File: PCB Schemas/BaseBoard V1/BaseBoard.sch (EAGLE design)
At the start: 31 parts, among them IC1 74HC595D, IC2 74HC595D, IC3 74HC595D, U1 ATMEGA2560AU, X1 16MHz

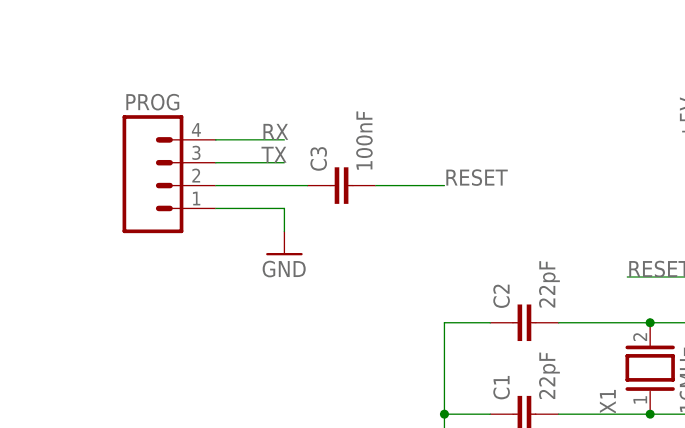
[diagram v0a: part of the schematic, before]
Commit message: Corrected BaseBoard V1 and updated license file
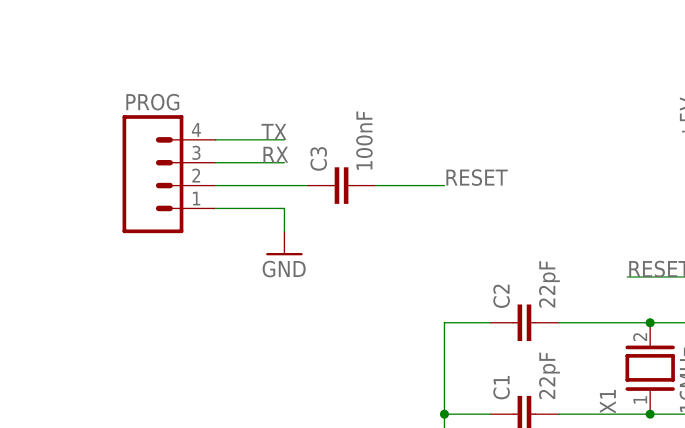
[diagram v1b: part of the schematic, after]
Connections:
- net RX: now also PROG.3; no longer PROG.4
- net TX: now also PROG.4; no longer PROG.3
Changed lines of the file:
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@@
 <net name="RX" class="0">
+<segment>
+<label x="132.08" y="-2.54" size="1.778" layer="95"/>
+<pinref part="U1" gate="1" pin="(RXD0/PCIN8)PE0"/>
+<wire x1="106.68" y1="-2.54" x2="132.08" y2="-2.54" width="0.1524" layer="91"/>
+</segment>
+<segment>
+<pinref part="PROG" gate="G$1" pin="3"/>
+<wire x1="-30.48" y1="119.38" x2="-22.86" y2="119.38" width="0.1524" layer="91"/>
+<label x="-25.4" y="119.38" size="1.778" layer="95"/>
+</segment>
+</net>
+<net name="TX" class="0">
+<segment>
+<label x="132.08" y="0" size="1.778" layer="95"/>
+<pinref part="U1" gate="1" pin="(TXD0)PE1"/>
+<wire x1="132.08" y1="0" x2="106.68" y2="0" width="0.1524" layer="91"/>
+</segment>
 <segment>
 <pinref part="PROG" gate="G$1" pin="4"/>
@@
 <label x="-25.4" y="121.92" size="1.778" layer="95"/>
 </segment>
-<segment>
-<label x="132.08" y="-2.54" size="1.778" layer="95"/>
-<pinref part="U1" gate="1" pin="(RXD0/PCIN8)PE0"/>
-<wire x1="106.68" y1="-2.54" x2="132.08" y2="-2.54" width="0.1524" layer="91"/>
-</segment>
 </net>
-<net name="TX" class="0">
-<segment>
-<pinref part="PROG" gate="G$1" pin="3"/>
-<wire x1="-30.48" y1="119.38" x2="-22.86" y2="119.38" width="0.1524" layer="91"/>
-<label x="-25.4" y="119.38" size="1.778" layer="95"/>
-</segment>
-<segment>
-<label x="132.08" y="0" size="1.778" layer="95"/>
-<pinref part="U1" gate="1" pin="(TXD0)PE1"/>
-<wire x1="132.08" y1="0" x2="106.68" y2="0" width="0.1524" layer="91"/>
-</segment>
-</net>

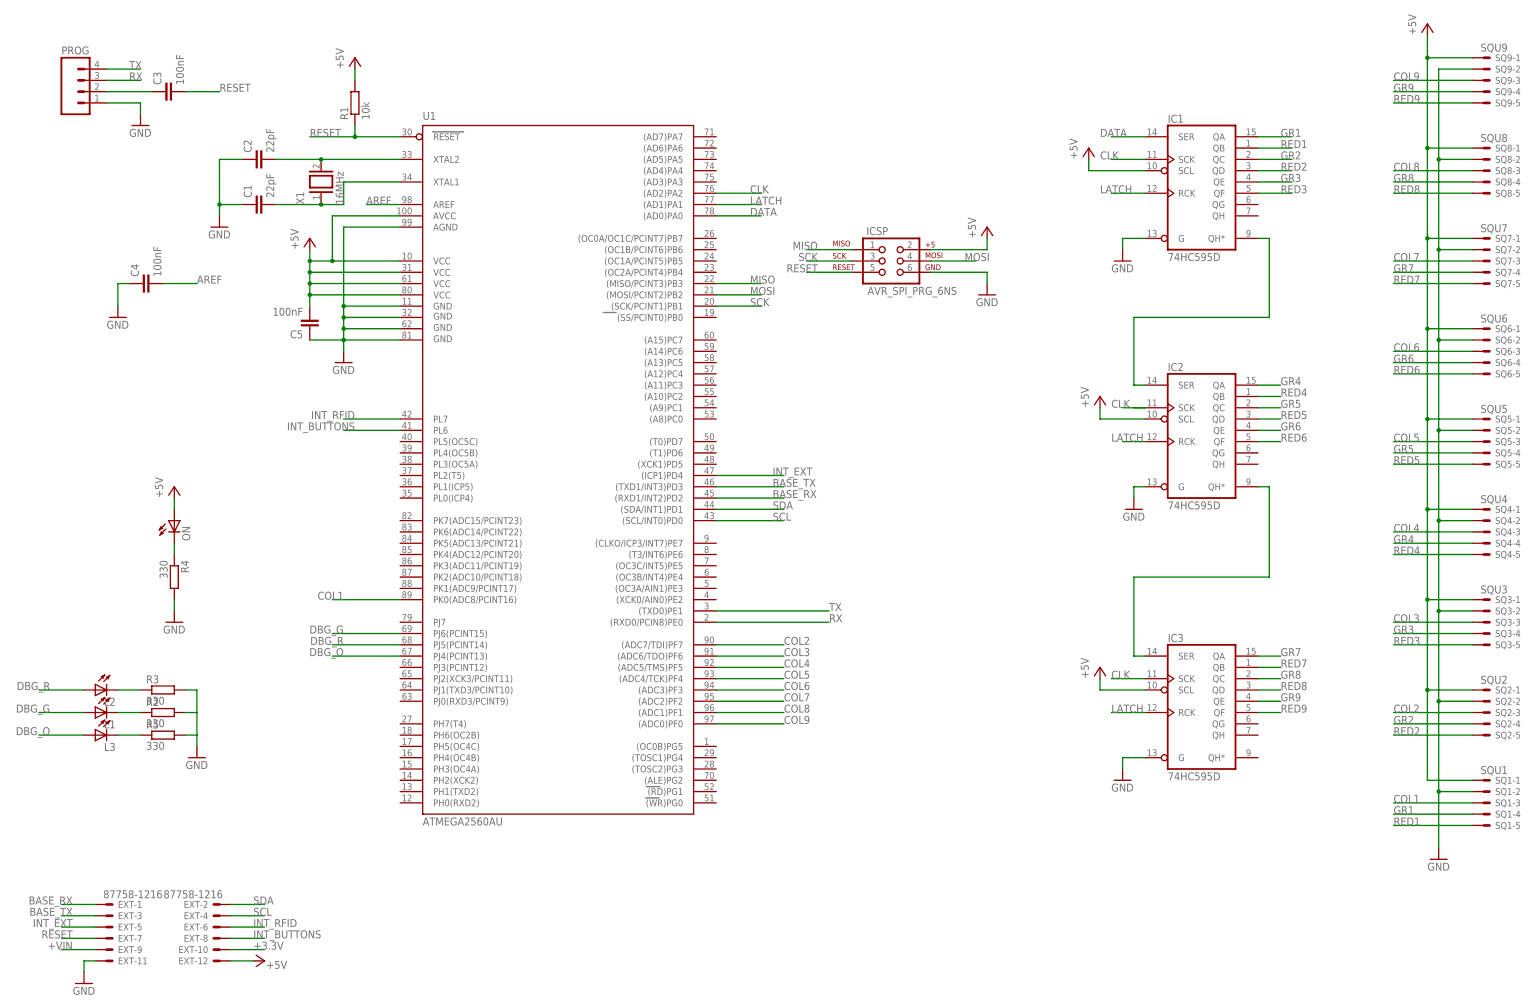
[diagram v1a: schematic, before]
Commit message: Modified base conector; delete reset pin
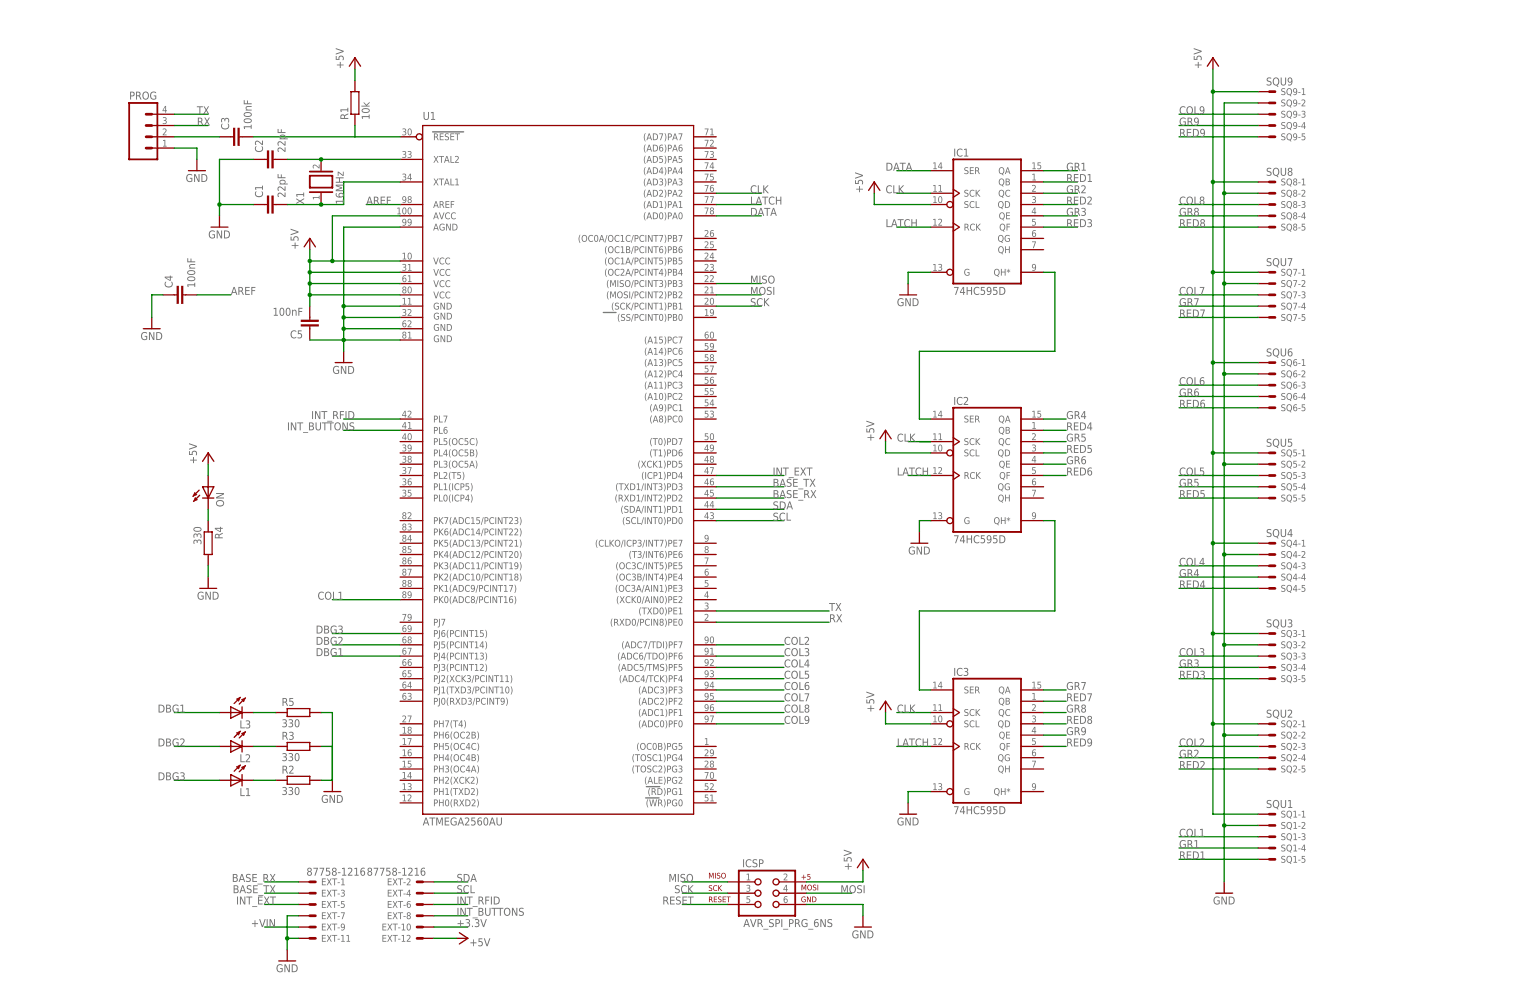
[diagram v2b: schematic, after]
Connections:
- net DBG_G renamed DBG3
- net DBG_O renamed DBG1
- net DBG_R renamed DBG2
- net GND: now also EXT-7.S
- net RESET: no longer EXT-7.S
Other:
- moved on the sheet: C1, C2, C3, C4, EXT-1, EXT-10, EXT-11, EXT-12, EXT-2, EXT-3, EXT-4, EXT-5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

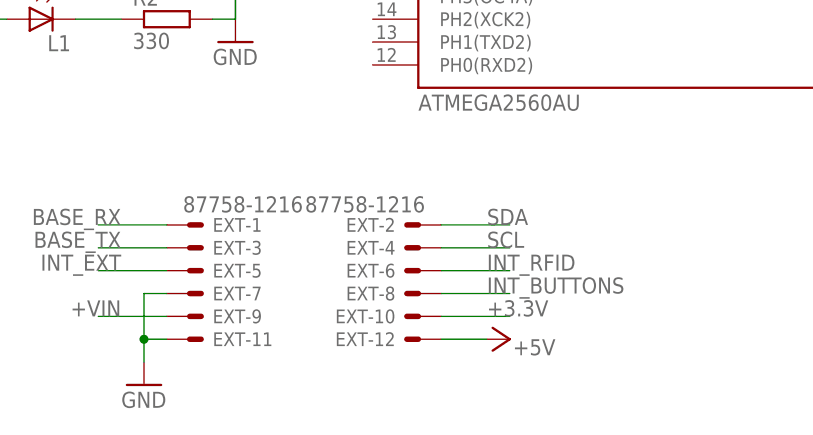
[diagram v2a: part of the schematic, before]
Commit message: Update base conector package
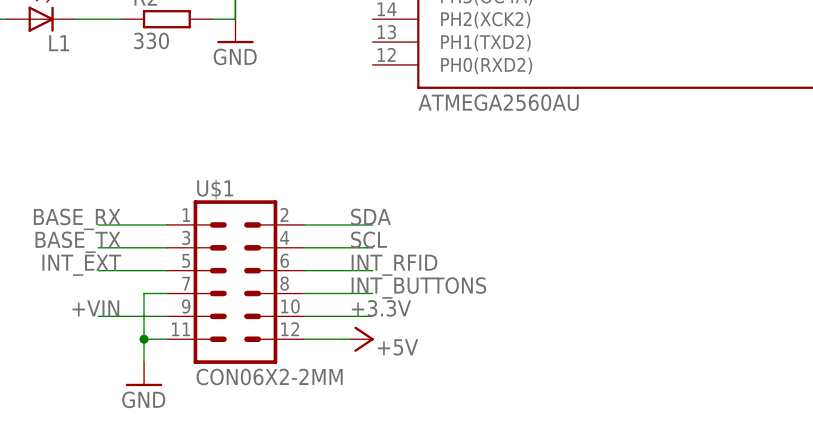
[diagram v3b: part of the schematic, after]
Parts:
- removed EXT: 87758-1216, con-molex:87758-1216
- added U$1: CON06X2-2MM, Connectors:CON06X2-2MM
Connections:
- net +3.3V: now also U$1.10; no longer EXT-10.S
- net +VIN: now also U$1.9; no longer EXT-9.S
- net BASE_RX: now also U$1.1; no longer EXT-1.S
- net BASE_TX: now also U$1.3; no longer EXT-3.S
- net GND: now also U$1.11, U$1.7; no longer EXT-11.S, EXT-7.S
- net INT_BUTTONS: now also U$1.8; no longer EXT-8.S
- net INT_EXT: now also U$1.5; no longer EXT-5.S
- net INT_RFID: now also U$1.6; no longer EXT-6.S
- net SCL: now also U$1.4; no longer EXT-4.S
- net SDA: now also U$1.2; no longer EXT-2.S
- net VCC: now also U$1.12; no longer EXT-12.S
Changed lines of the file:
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@@
 <part name="GND5" library="supply1" deviceset="GND" device=""/>
 <part name="P+3" library="supply1" deviceset="VCC" device="" value="+5V"/>
-<part name="EXT" library="con-molex" deviceset="87758-1216" device=""/>
 <part name="R2" library="resistor" deviceset="R-EU_" device="R0805" value="330"/>
 <part name="R3" library="resistor" deviceset="R-EU_" device="R0805" value="330"/>
@@
 <part name="L1" library="led" deviceset="LED" device="CHIP-LED0805"/>
 <part name="L3" library="led" deviceset="LED" device="CHIP-LED0805"/>
+<part name="U$1" library="Connectors" deviceset="CON06X2-2MM" device=""/>
 </parts>
 <sheets>
@@
 <instance part="GND11" gate="1" x="149.86" y="-45.72"/>
 <instance part="GND12" gate="1" x="10.16" y="-78.74"/>
-<instance part="P+9" gate="VCC" x="50.8" y="-73.66" smashed="yes" rot="R270">
-<attribute name="VALUE" x="55.88" y="-73.66" size="1.778" layer="96" rot="R180"/>
+<instance part="P+9" gate="VCC" x="35.56" y="-73.66" smashed="yes" rot="R270">
+<attribute name="VALUE" x="40.64" y="-73.66" size="1.778" layer="96" rot="R180"/>
 </instance>
 <instance part="ICSP" gate="G$1" x="116.84" y="-63.5"/>
 <instance part="GND5" gate="1" x="139.7" y="-71.12"/>
 <instance part="P+3" gate="VCC" x="139.7" y="-55.88"/>
-<instance part="EXT" gate="-1" x="15.24" y="-60.96"/>
-<instance part="EXT" gate="-2" x="40.64" y="-60.96" rot="MR0"/>
-<instance part="EXT" gate="-3" x="15.24" y="-63.5"/>
-<instance part="EXT" gate="-4" x="40.64" y="-63.5" rot="MR0"/>
-<instance part="EXT" gate="-5" x="15.24" y="-66.04"/>
-<instance part="EXT" gate="-6" x="40.64" y="-66.04" rot="MR0"/>
-<instance part="EXT" gate="-7" x="15.24" y="-68.58"/>
-<instance part="EXT" gate="-8" x="40.64" y="-68.58" rot="MR0"/>
-<instance part="EXT" gate="-9" x="15.24" y="-71.12"/>
-<instance part="EXT" gate="-10" x="40.64" y="-71.12" rot="MR0"/>
-<instance part="EXT" gate="-11" x="15.24" y="-73.66"/>
-<instance part="EXT" gate="-12" x="40.64" y="-73.66" rot="MR0"/>
 <instance part="R2" gate="G$1" x="12.7" y="-38.1"/>
 <instance part="R3" gate="G$1" x="12.7" y="-30.48"/>
@@
 <instance part="L1" gate="G$1" x="-2.54" y="-38.1" rot="MR270"/>
 <instance part="L3" gate="G$1" x="-2.54" y="-22.86" rot="MR270"/>
+<instance part="U$1" gate="G$1" x="20.32" y="-68.58"/>
 </instances>
 <busses>
@@
 <segment>
 <pinref part="P+9" gate="VCC" pin="VCC"/>
-<wire x1="43.18" y1="-73.66" x2="48.26" y2="-73.66" width="0.1524" layer="91"/>
-<pinref part="EXT" gate="-12" pin="S"/>
+<wire x1="27.94" y1="-73.66" x2="33.02" y2="-73.66" width="0.1524" layer="91"/>
+<pinref part="U$1" gate="G$1" pin="12"/>
 </segment>
 </net>
@@
 <wire x1="12.7" y1="-73.66" x2="10.16" y2="-73.66" width="0.1524" layer="91"/>
 <wire x1="10.16" y1="-73.66" x2="10.16" y2="-76.2" width="0.1524" layer="91"/>
-<pinref part="EXT" gate="-11" pin="S"/>
-<pinref part="EXT" gate="-7" pin="S"/>
 <wire x1="12.7" y1="-68.58" x2="10.16" y2="-68.58" width="0.1524" layer="91"/>
 <wire x1="10.16" y1="-68.58" x2="10.16" y2="-73.66" width="0.1524" layer="91"/>
 <junction x="10.16" y="-73.66"/>
+<pinref part="U$1" gate="G$1" pin="7"/>
+<pinref part="U$1" gate="G$1" pin="11"/>
 </segment>
 </net>
@@
 </segment>
 <segment>
-<wire x1="43.18" y1="-63.5" x2="50.8" y2="-63.5" width="0.1524" layer="91"/>
-<label x="48.26" y="-63.5" size="1.778" layer="95"/>
-<pinref part="EXT" gate="-4" pin="S"/>
+<wire x1="27.94" y1="-63.5" x2="35.56" y2="-63.5" width="0.1524" layer="91"/>
+<label x="33.02" y="-63.5" size="1.778" layer="95"/>
+<pinref part="U$1" gate="G$1" pin="4"/>
 </segment>
 </net>
@@
 </segment>
 <segment>
-<wire x1="43.18" y1="-60.96" x2="50.8" y2="-60.96" width="0.1524" layer="91"/>
-<label x="48.26" y="-60.96" size="1.778" layer="95"/>
-<pinref part="EXT" gate="-2" pin="S"/>
+<wire x1="27.94" y1="-60.96" x2="35.56" y2="-60.96" width="0.1524" layer="91"/>
+<label x="33.02" y="-60.96" size="1.778" layer="95"/>
+<pinref part="U$1" gate="G$1" pin="2"/>
 </segment>
 </net>
@@
 <wire x1="12.7" y1="-63.5" x2="5.08" y2="-63.5" width="0.1524" layer="91"/>
 <label x="7.62" y="-63.5" size="1.778" layer="95" rot="MR0"/>
-<pinref part="EXT" gate="-3" pin="S"/>
+<pinref part="U$1" gate="G$1" pin="3"/>
 </segment>
 </net>
@@
 <wire x1="12.7" y1="-60.96" x2="5.08" y2="-60.96" width="0.1524" layer="91"/>
 <label x="7.62" y="-60.96" size="1.778" layer="95" rot="MR0"/>
-<pinref part="EXT" gate="-1" pin="S"/>
+<pinref part="U$1" gate="G$1" pin="1"/>
 </segment>
 </net>
@@
 </segment>
 <segment>
-<wire x1="43.18" y1="-66.04" x2="50.8" y2="-66.04" width="0.1524" layer="91"/>
-<label x="48.26" y="-66.04" size="1.778" layer="95"/>
-<pinref part="EXT" gate="-6" pin="S"/>
+<wire x1="27.94" y1="-66.04" x2="35.56" y2="-66.04" width="0.1524" layer="91"/>
+<label x="33.02" y="-66.04" size="1.778" layer="95"/>
+<pinref part="U$1" gate="G$1" pin="6"/>
 </segment>
 </net>
@@
 </segment>
 <segment>
-<wire x1="43.18" y1="-68.58" x2="50.8" y2="-68.58" width="0.1524" layer="91"/>
-<label x="48.26" y="-68.58" size="1.778" layer="95"/>
-<pinref part="EXT" gate="-8" pin="S"/>
+<wire x1="27.94" y1="-68.58" x2="35.56" y2="-68.58" width="0.1524" layer="91"/>
+<label x="33.02" y="-68.58" size="1.778" layer="95"/>
+<pinref part="U$1" gate="G$1" pin="8"/>
 </segment>
 </net>
@@
 <net name="INT_EXT" class="0">
 <segment>
-<pinref part="EXT" gate="-5" pin="S"/>
 <wire x1="12.7" y1="-66.04" x2="5.08" y2="-66.04" width="0.1524" layer="91"/>
 <label x="7.62" y="-66.04" size="1.778" layer="95" rot="MR0"/>
+<pinref part="U$1" gate="G$1" pin="5"/>
 </segment>
 <segment>
@@
 <net name="+3.3V" class="0">
 <segment>
-<wire x1="43.18" y1="-71.12" x2="50.8" y2="-71.12" width="0.1524" layer="91"/>
-<label x="48.26" y="-71.12" size="1.778" layer="95"/>
-<pinref part="EXT" gate="-10" pin="S"/>
+<wire x1="27.94" y1="-71.12" x2="35.56" y2="-71.12" width="0.1524" layer="91"/>
+<label x="33.02" y="-71.12" size="1.778" layer="95"/>
+<pinref part="U$1" gate="G$1" pin="10"/>
 </segment>
 </net>
@@
 <wire x1="12.7" y1="-71.12" x2="5.08" y2="-71.12" width="0.1524" layer="91"/>
 <label x="7.62" y="-71.12" size="1.778" layer="95" rot="MR0"/>
-<pinref part="EXT" gate="-9" pin="S"/>
-</segment>
-</net>
+<pinref part="U$1" gate="G$1" pin="9"/>
+</segment>
+</net>

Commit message: Updated details
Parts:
- C1: value 22pF -> 100nF
- C3: value 100nF -> 22pF
- IC1: value 74HC595D -> ATMEGA2560AU; device 74xx-eu:74HC595D -> SparkFun-DigitalIC:ATMEGA2560AU
- J1: value (none) -> PROGRAM
- U1: value ATMEGA2560AU -> 74HC595D; device SparkFun-DigitalIC:ATMEGA2560AU -> 74xx-eu:74HC595D
- renumbered IC2 to U2, IC3 to U3, PROG to J1, SQ1 to S1, SQ2 to S2, SQ3 to S3, SQ4 to S4, SQ5 to S5, SQ6 to S6, SQ7 to S7, SQ8 to S8, SQ9 to S9, U$1 to J2
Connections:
- removed net N$4 (its old number): L1.C, R2.1
- new net N$9: L1.C, R3.1
- net +VIN: now also J2.7; no longer J2.9
- net AREF: now also IC1.AREF; no longer U1.AREF
- net BASE_RX: now also IC1.(RXD1/INT2)PD2; no longer U1.(RXD1/INT2)PD2
- net BASE_TX: now also IC1.(TXD1/INT3)PD3; no longer U1.(TXD1/INT3)PD3
- net CLK: now also IC1.(AD2)PA2, U1A.SCK; no longer IC1A.SCK, U1.(AD2)PA2
- net COL1: now also IC1.PK0(ADC8/PCINT16); no longer U1.PK0(ADC8/PCINT16)
- net COL2: now also IC1.(ADC7/TDI)PF7; no longer U1.(ADC7/TDI)PF7
- net COL3: now also IC1.(ADC6/TDO)PF6; no longer U1.(ADC6/TDO)PF6
- net COL4: now also IC1.(ADC5/TMS)PF5; no longer U1.(ADC5/TMS)PF5
- net COL5: now also IC1.(ADC4/TCK)PF4; no longer U1.(ADC4/TCK)PF4
- net COL6: now also IC1.(ADC3)PF3; no longer U1.(ADC3)PF3
- net COL7: now also IC1.(ADC2)PF2; no longer U1.(ADC2)PF2
- net COL8: now also IC1.(ADC1)PF1; no longer U1.(ADC1)PF1
- net COL9: now also IC1.(ADC0)PF0; no longer U1.(ADC0)PF0
- net DATA: now also IC1.(AD0)PA0, U1A.SER; no longer IC1A.SER, U1.(AD0)PA0
- net DBG1: now also IC1.PJ4(PCINT13), L1.A; no longer L3.A, U1.PJ4(PCINT13)
- net DBG2: now also IC1.PJ5(PCINT14); no longer U1.PJ5(PCINT14)
- net DBG3: now also IC1.PJ6(PCINT15), L3.A; no longer L1.A, U1.PJ6(PCINT15)
- net GND: now also C3.1, IC1.AGND, IC1.GND, IC1.GND1, IC1.GND2, IC1.GND3, J2.9, U1A.G; no longer C1.1, IC1A.G, J2.7, U1.AGND, U1.GND, U1.GND1, U1.GND2, U1.GND3
- net GR1: now also U1A.QA; no longer IC1A.QA
- net GR2: now also U1A.QC; no longer IC1A.QC
- net GR3: now also U1A.QE; no longer IC1A.QE
- net INT_BUTTONS: now also IC1.PL6; no longer U1.PL6
- net INT_EXT: now also IC1.(ICP1)PD4; no longer U1.(ICP1)PD4
- net INT_RFID: now also IC1.PL7; no longer U1.PL7
- net LATCH: now also IC1.(AD1)PA1, U1A.RCK; no longer IC1A.RCK, U1.(AD1)PA1
- net MISO: now also IC1.(MISO/PCINT3)PB3; no longer U1.(MISO/PCINT3)PB3
- net MOSI: now also IC1.(MOSI/PCINT2)PB2; no longer U1.(MOSI/PCINT2)PB2
- net N$1: now also IC1.XTAL2; no longer U1.XTAL2
- net N$2: now also C3.2, IC1.XTAL1; no longer C1.2, U1.XTAL1
- net N$3: now also R4.1; no longer R3.1
- net N$5: now also C1.1; no longer C3.1
- net N$6: now also U1A.QH*; no longer IC1A.QH*
- net N$8: now also R2.1; no longer R4.1
- net RED1: now also U1A.QB; no longer IC1A.QB
- net RED2: now also U1A.QD; no longer IC1A.QD
- net RED3: now also U1A.QF; no longer IC1A.QF
- net RESET: now also C1.2, IC1.RESET; no longer C3.2, U1.RESET
- net RX: now also IC1.(RXD0/PCIN8)PE0; no longer U1.(RXD0/PCIN8)PE0
- net SCK: now also IC1.(SCK/PCINT1)PB1; no longer U1.(SCK/PCINT1)PB1
- net SCL: now also IC1.(SCL/INT0)PD0; no longer U1.(SCL/INT0)PD0
- net SDA: now also IC1.(SDA/INT1)PD1; no longer U1.(SDA/INT1)PD1
- net TX: now also IC1.(TXD0)PE1; no longer U1.(TXD0)PE1
- net VCC: now also IC1.AVCC, IC1.VCC, IC1.VCC1, IC1.VCC2, IC1.VCC3, U1A.SCL; no longer IC1A.SCL, U1.AVCC, U1.VCC, U1.VCC1, U1.VCC2, U1.VCC3
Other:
- moved on the sheet: C1, C3, C5, L1, L3, R2, R3, R4, R5

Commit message: Revised PCB schemas
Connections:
- net +3.3V: now also J2.5; no longer J2.10
- net +VIN: now also J2.9; no longer J2.7
- net BASE_RX: now also IC1.(TXD1/INT3)PD3, J2.3; no longer IC1.(RXD1/INT2)PD2, J2.1
- net BASE_TX: now also IC1.(RXD1/INT2)PD2, J2.1; no longer IC1.(TXD1/INT3)PD3, J2.3
- net DBG1: now also L3.A; no longer L1.A
- net DBG3: now also L1.A; no longer L3.A
- net GND: now also J2.12; no longer J2.9
- net INT_EXT: now also IC1.PL5(OC5C), J2.10; no longer IC1.(ICP1)PD4, J2.5
- net VCC: now also J2.7; no longer J2.12
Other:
- note added: "+5V"
- note added: "CONNECTED"
- moved on the sheet: ICSP, J2, L1, L2, L3, ON, R2, R3, R4, R5, S1-1, S1-2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
